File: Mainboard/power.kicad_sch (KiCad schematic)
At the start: 14 parts, among them J101 9V IN, U101 MIC29302WU

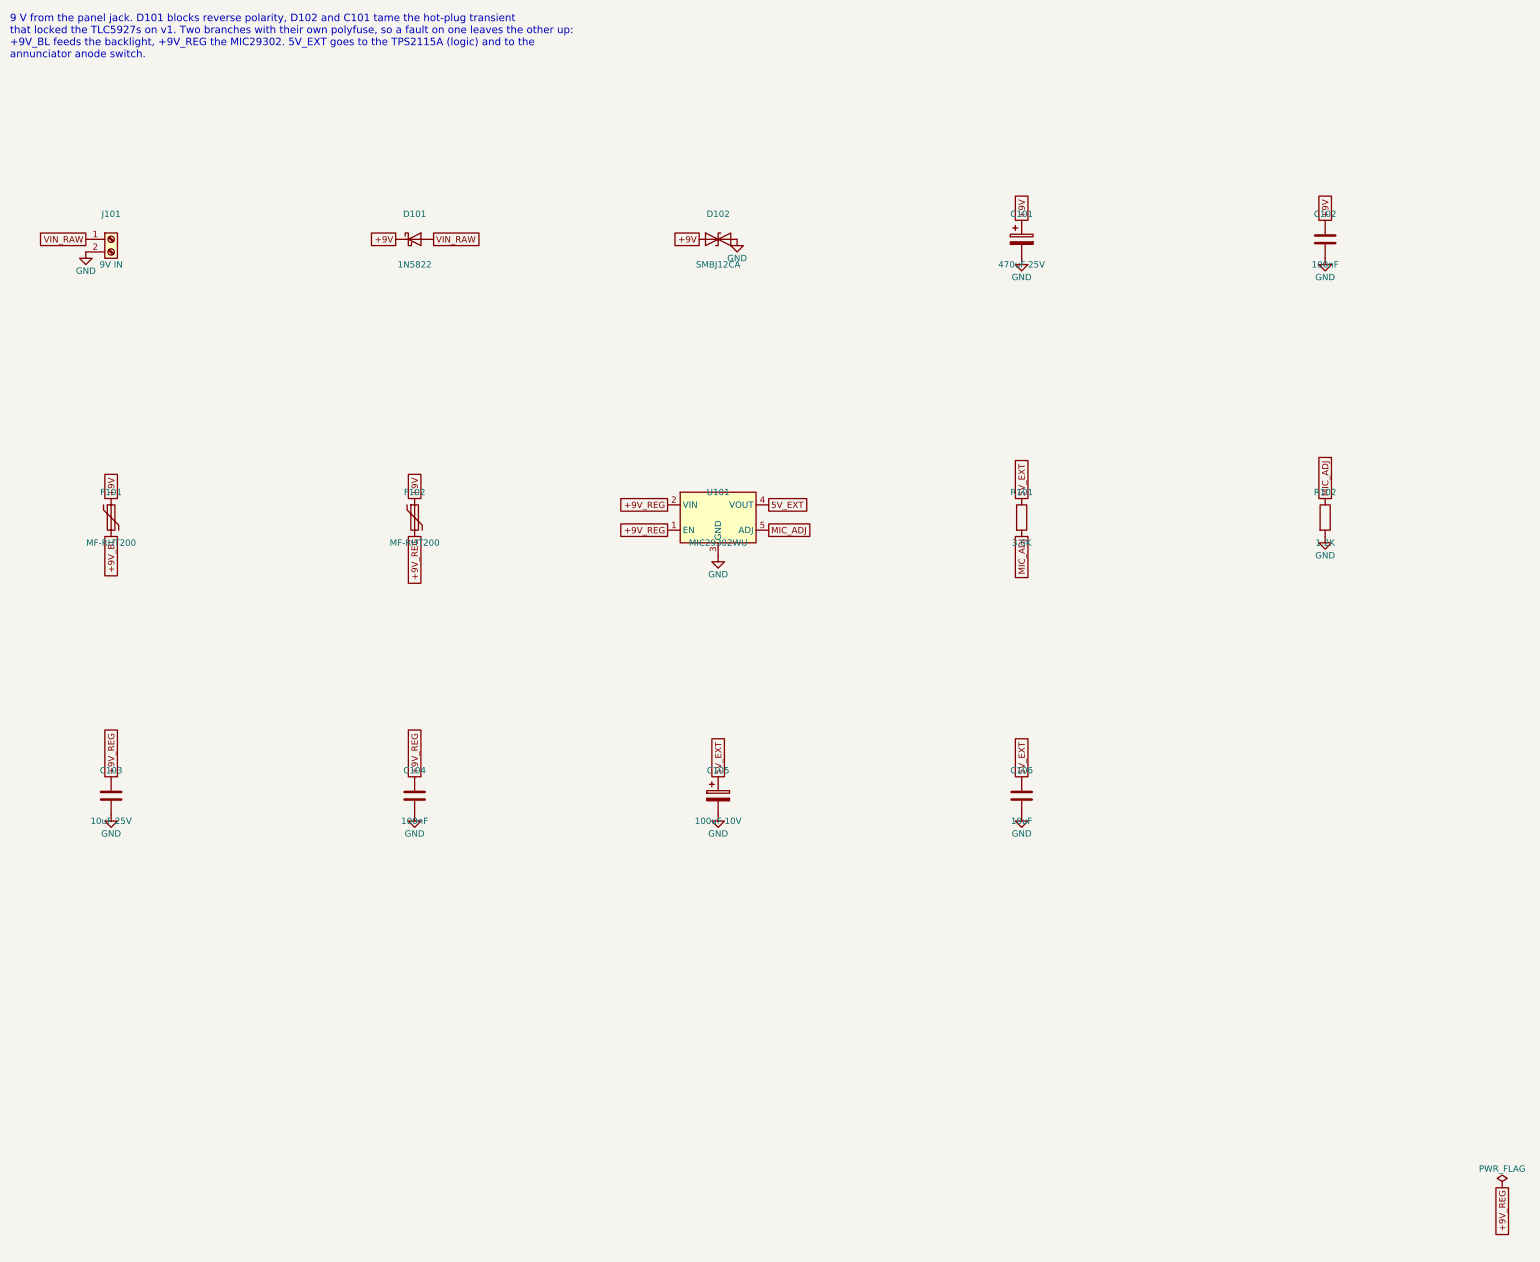
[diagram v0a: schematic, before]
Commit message: Lay the mainboard schematic out so that nothing overlaps
Reference and value now sit outside each symbol (above and below, or beside
it for parts whose pins leave up and down), turned horizontal on rotated
parts. GND on a sideways pin is a label instead of a power symbol that
crowded the neighbouring pins. The annunciator sheet keeps its four TLC5927
in two wider columns, their R-EXT and capacitors in a row underneath, the
series resistors horizontal on the right and both supply switches along the
bottom, all inside the frame. The connector sheet has wider columns.

Layout only: the netlist is identical to the previous commit (126 parts,
230 nets, same values, footprints and fields), and ERC is still clean.

Co-Authored-By: Claude Opus 5.5 <noreply@anthropic.com>
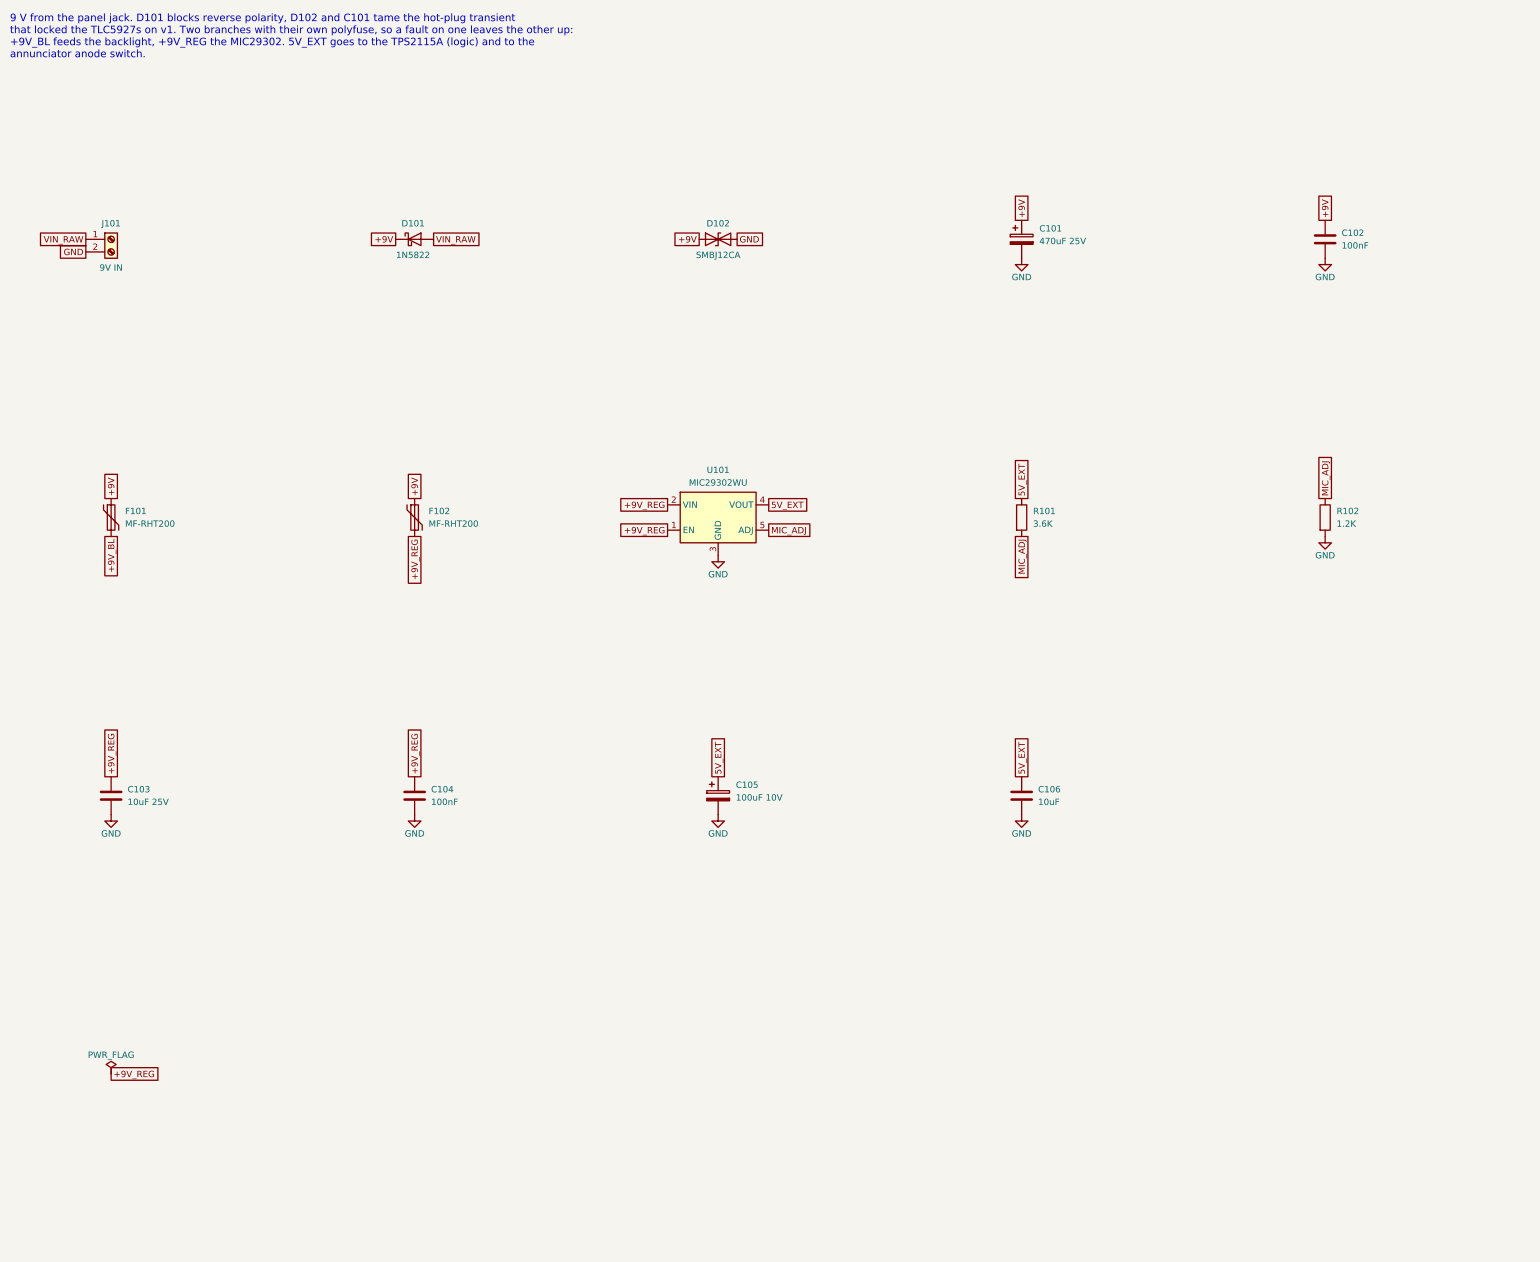
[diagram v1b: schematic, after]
